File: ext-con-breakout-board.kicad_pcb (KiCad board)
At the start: 4 copper layers, 46 x 36.6 mm, 7 parts, among them J1 Conn_02x12_Odd_Even, J2 Conn_01x16

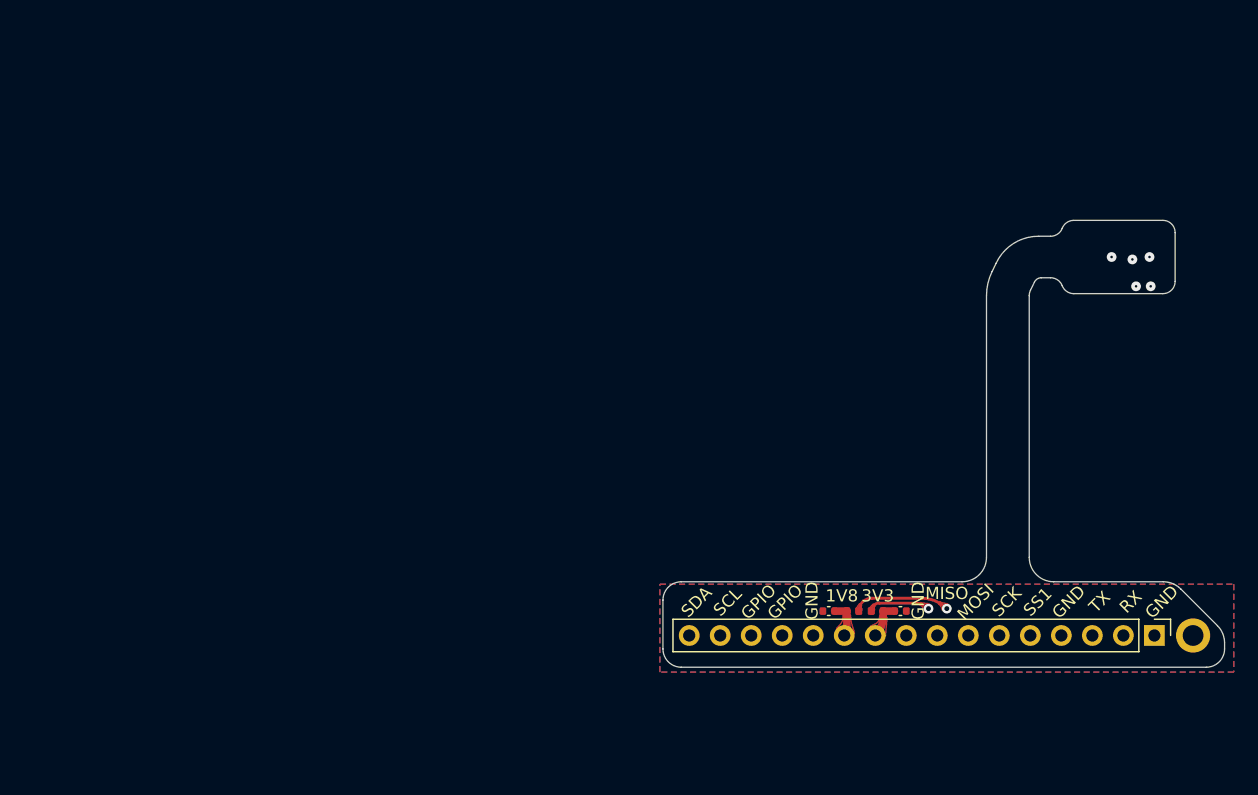
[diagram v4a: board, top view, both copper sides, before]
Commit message: Export the manufacturing files (gerbers and PDF)
Add fab notes on the User.Comments layer. Include a general stackup
guide image in the PDF fabrication drawing.

Re-centered the whole board on the canvas. The vias on the flex section
have to be set as "buried" vias going from In1.Cu to In2.Cu in order to
get the correct gerber export.
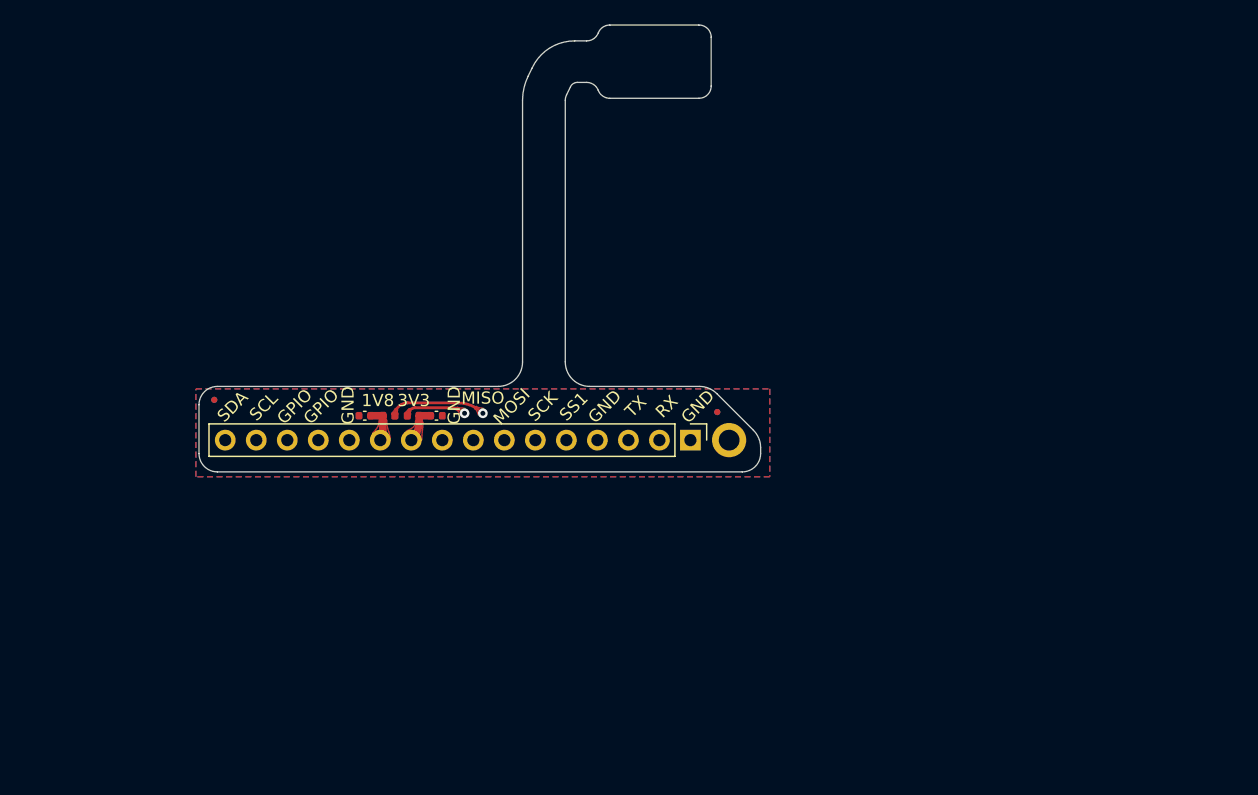
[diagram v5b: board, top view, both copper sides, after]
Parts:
- added FID1: Fiducial, ext-con-breakout-board:Fiducial_0.5mm_Mask1mm, F.Cu at (96.5, 115.7)
- added FID2: Fiducial, ext-con-breakout-board:Fiducial_0.5mm_Mask1mm, F.Cu at (137.7, 116.7)
- moved C2 41.2 mm to (108.8, 117.0)
- moved FB1 41.2 mm to (112.8, 117.0)
- moved FB2 41.2 mm to (110.8, 117.0)
- moved H1 41.2 mm to (138.7, 119.0)
- moved J1 41.2 mm to (133.0, 88.0)
- moved J2 41.2 mm to (135.5, 119.0)
- moved C1 41.2 mm to (114.7, 117.0)
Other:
- board text added: "1. THIS BOARD SHALL CONFORM TO: IPC-6013, CURRENT REVISION, CLASS II IPC-A-600, CURRENT REVISION, CLASS II. 2. OVERALL RIGID BOARD THICKNESS SHALL BE 1.60mm +/-10%. 3. FLEX SECTION SHALL USE A POLYIMIDE CORE SUBSTRATE MATERIAL AND A POLYIMIDE COVERLAY SURFACE. 4. APPLY KAPTON STIFFENER TO THE DESIGNATED SECTION OF THE FLEX. 5. APPLY SOLDERMASK OVER RIGID SECTION, COLOR BLACK; MASK SHALL MEET IPC-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"
- board text added: "NOTE: UNLESS OTHERWISE SPECIFIED"

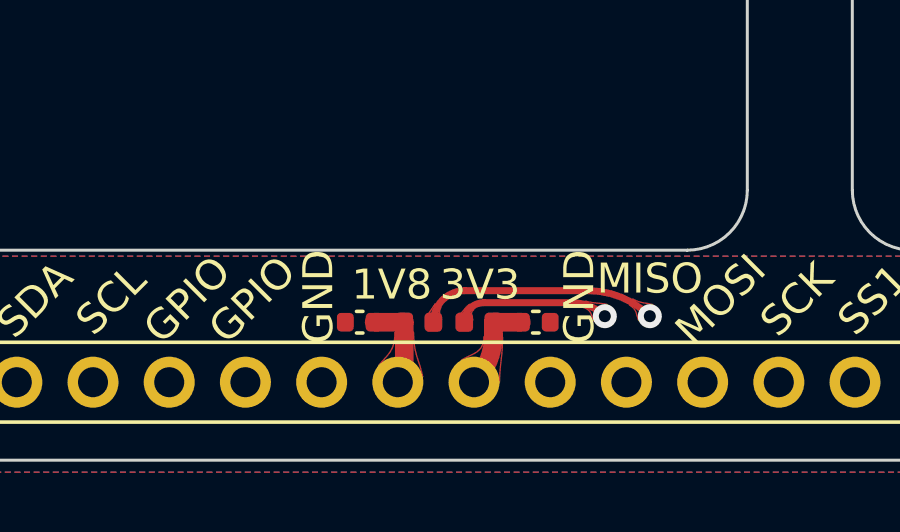
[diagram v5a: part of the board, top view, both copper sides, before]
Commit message: Fix the SPI_SCK and SPI_SS1 traces having slight kinks on the straight long flex section
Re-export the gerbers after this fix is applied.
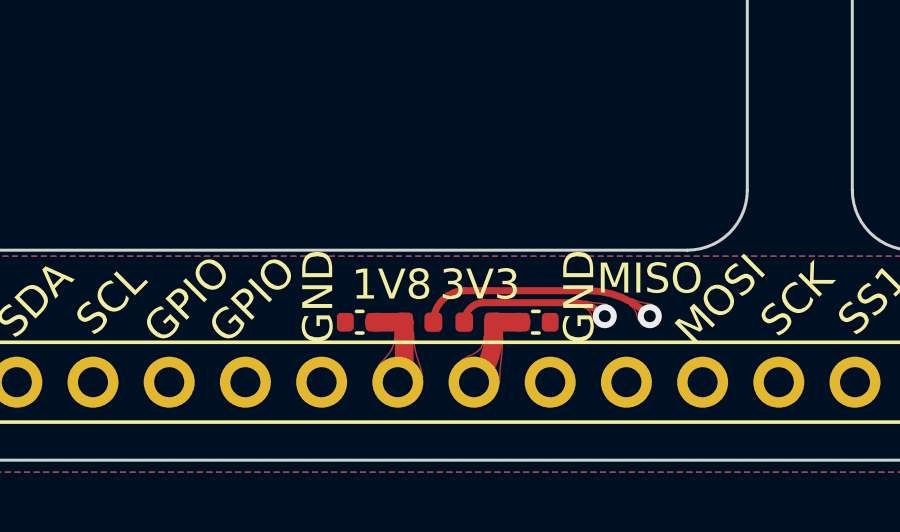
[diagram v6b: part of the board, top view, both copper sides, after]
